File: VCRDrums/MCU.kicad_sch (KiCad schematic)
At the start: 45 parts, among them J901 SWD Header, SW901 RST, SW902 BOOT, U901 STM32F411RETx, Y901 16MHz, Y902 32.768kHZ

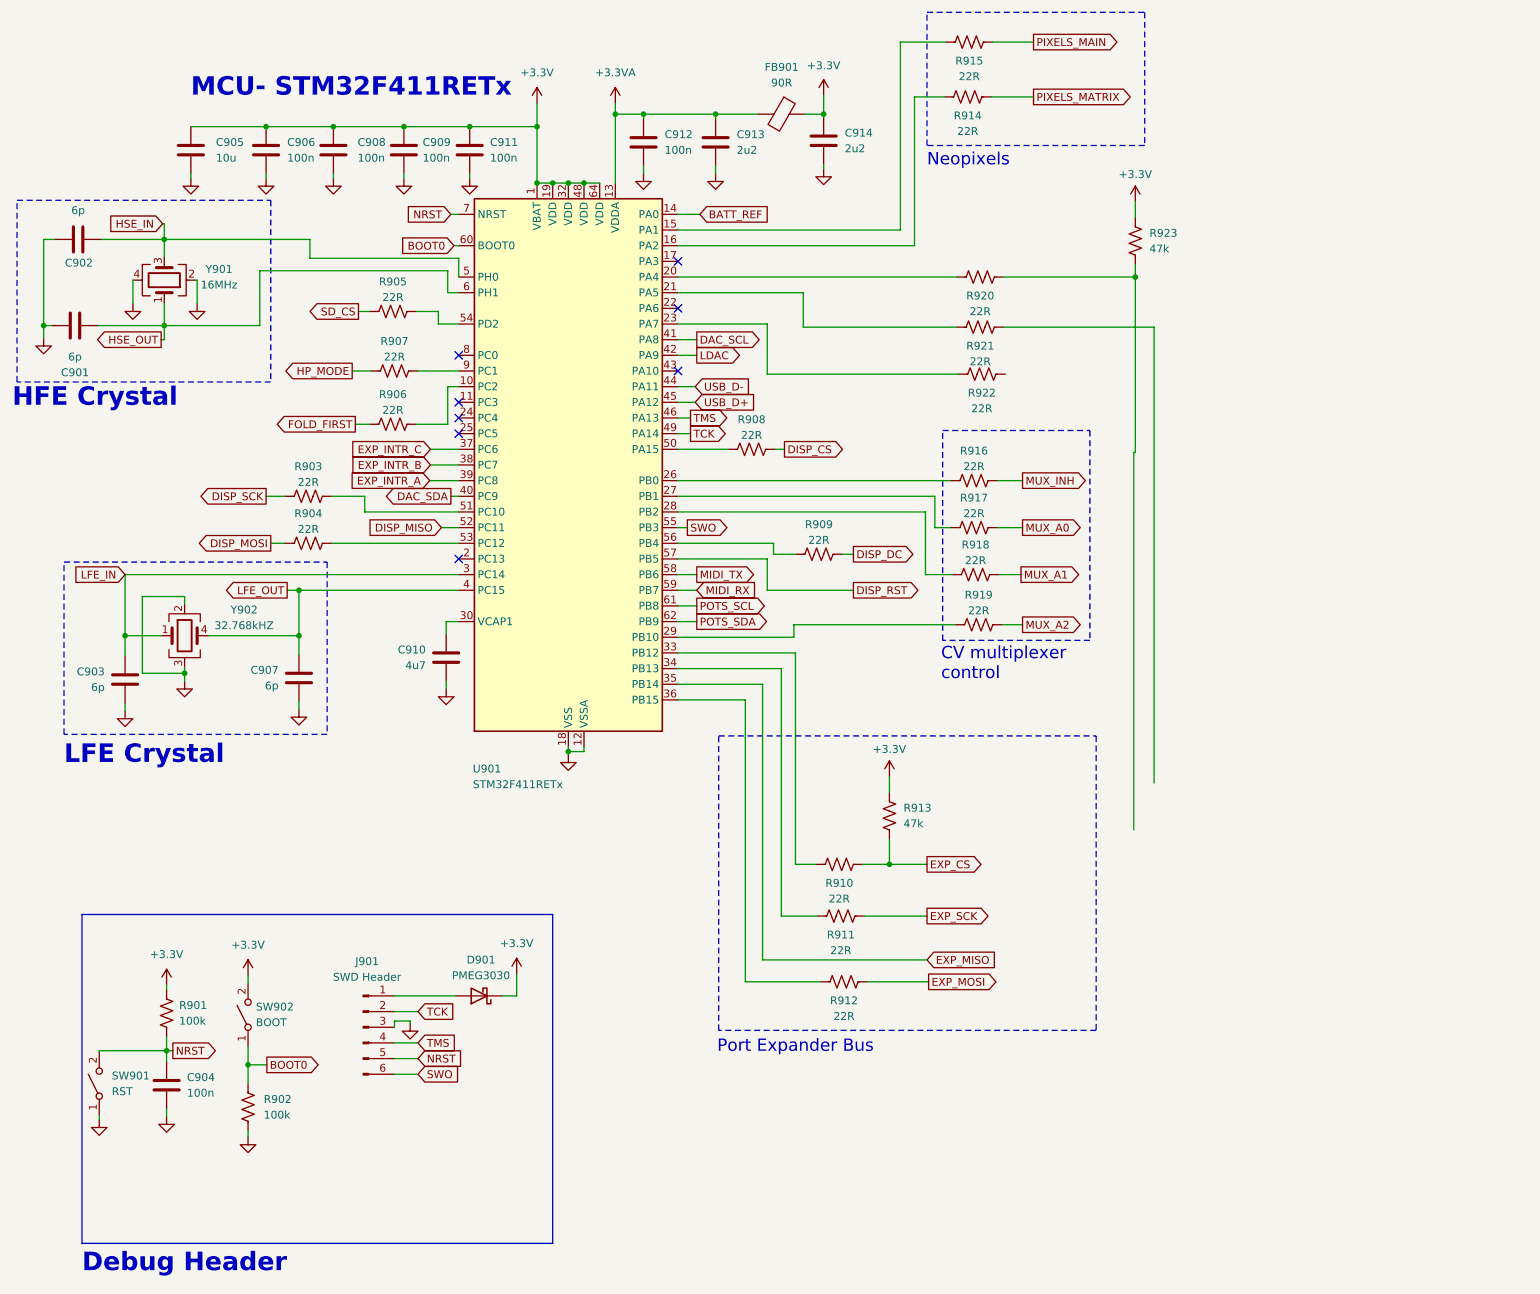
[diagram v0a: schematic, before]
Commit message: firmware boilerplate
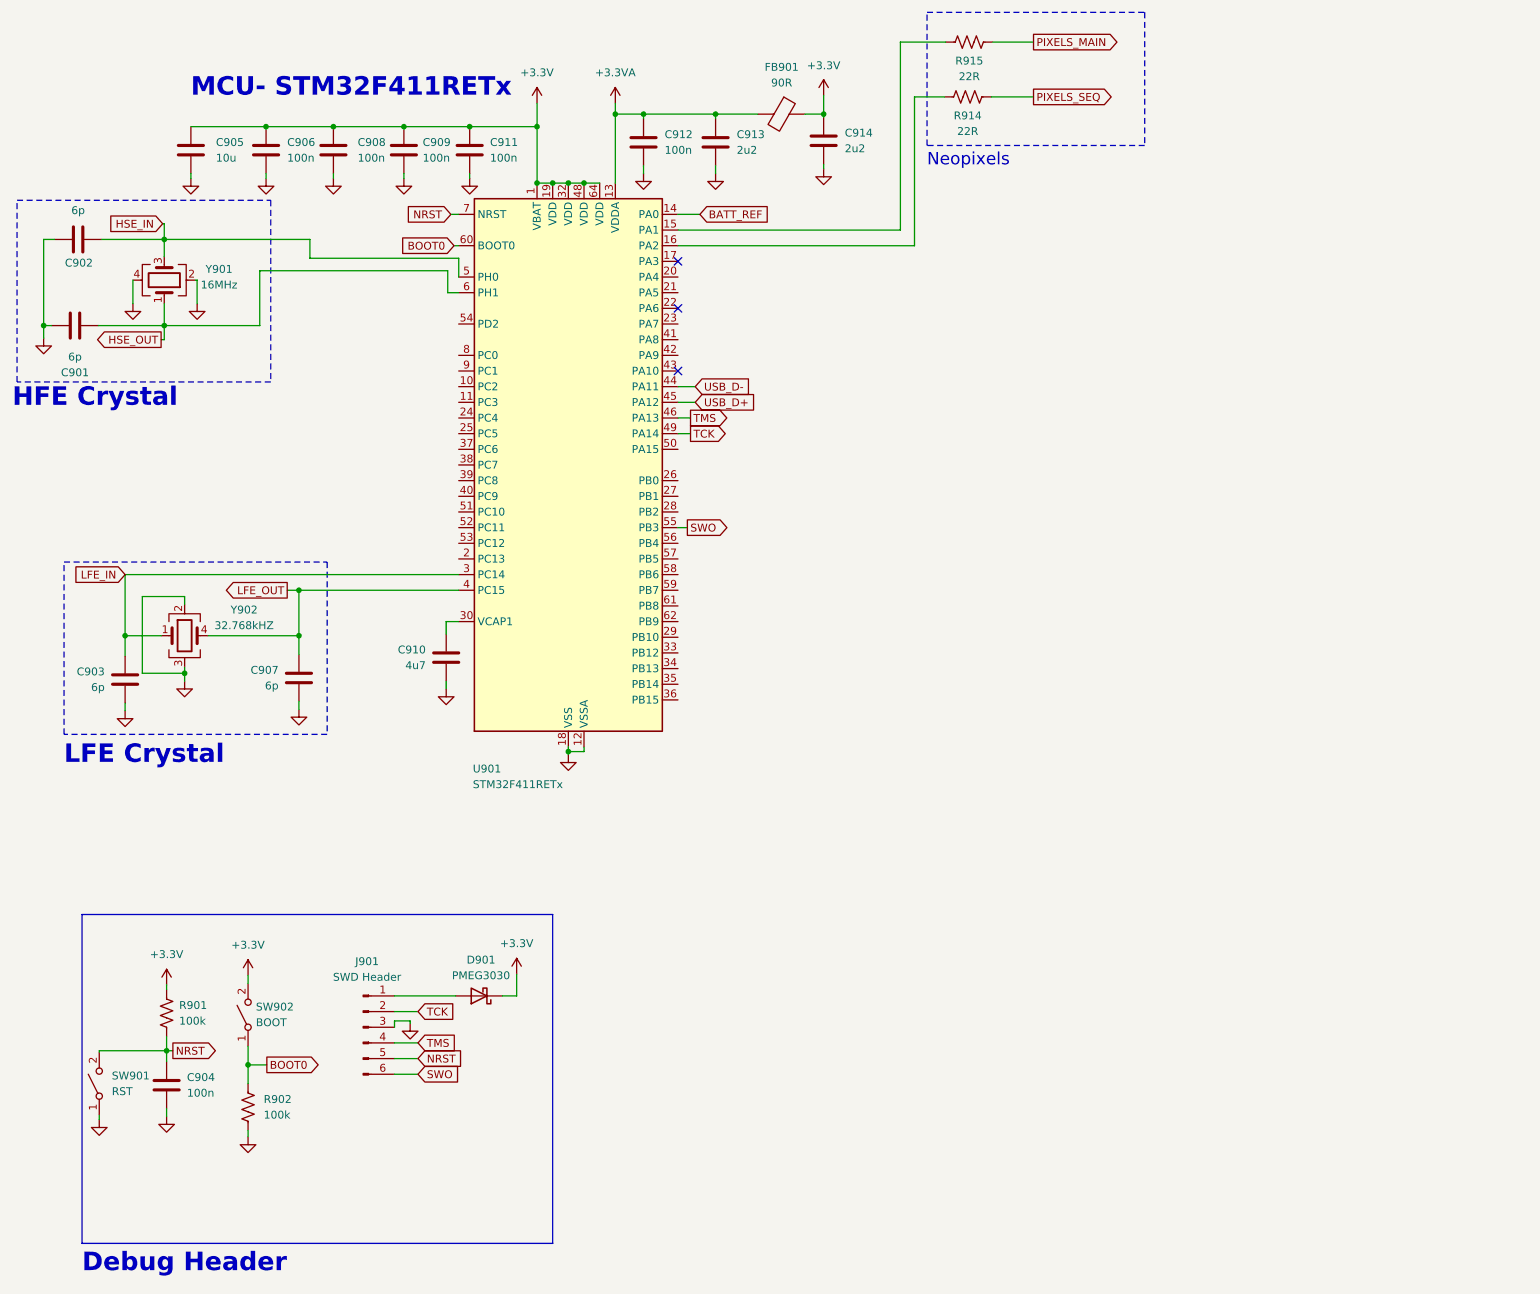
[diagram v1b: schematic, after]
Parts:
- removed R903, R904, R905, R906, R907, R908, R909, R910, R911, R912, R916, R917, R918, R919, R920, R921, R922: 22R, Resistor_SMD:R_0805_2012Metric, symbol Device:R_US
- removed R913, R923: 47k, Resistor_SMD:R_0805_2012Metric, symbol Device:R_US
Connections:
- net DAC_SCL: no longer names the net of U901.41 (PA8)
- net DAC_SDA: no longer names the net of U901.40 (PC9)
- net DISP_MISO: no longer names the net of U901.52 (PC11)
- net DISP_RST: no longer names the net of U901.57 (PB5)
- net EXP_INTR_A: no longer names the net of U901.39 (PC8)
- net EXP_INTR_B: no longer names the net of U901.38 (PC7)
- net EXP_INTR_C: no longer names the net of U901.37 (PC6)
- net EXP_MISO: no longer names the net of U901.35 (PB14)
- net LDAC: no longer names the net of U901.42 (PA9)
- net MIDI_RX: no longer names the net of U901.59 (PB7)
- net MIDI_TX: no longer names the net of U901.58 (PB6)
- net PIXELS_MATRIX renamed PIXELS_SEQ
- net POTS_SCL: no longer names the net of U901.61 (PB8)
- net POTS_SDA: no longer names the net of U901.62 (PB9)
- no-connect marks 8 -> 3
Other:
- note removed: "CV multiplexer control"
- note removed: "Port Expander Bus"

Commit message: compressor muxes and balanced out
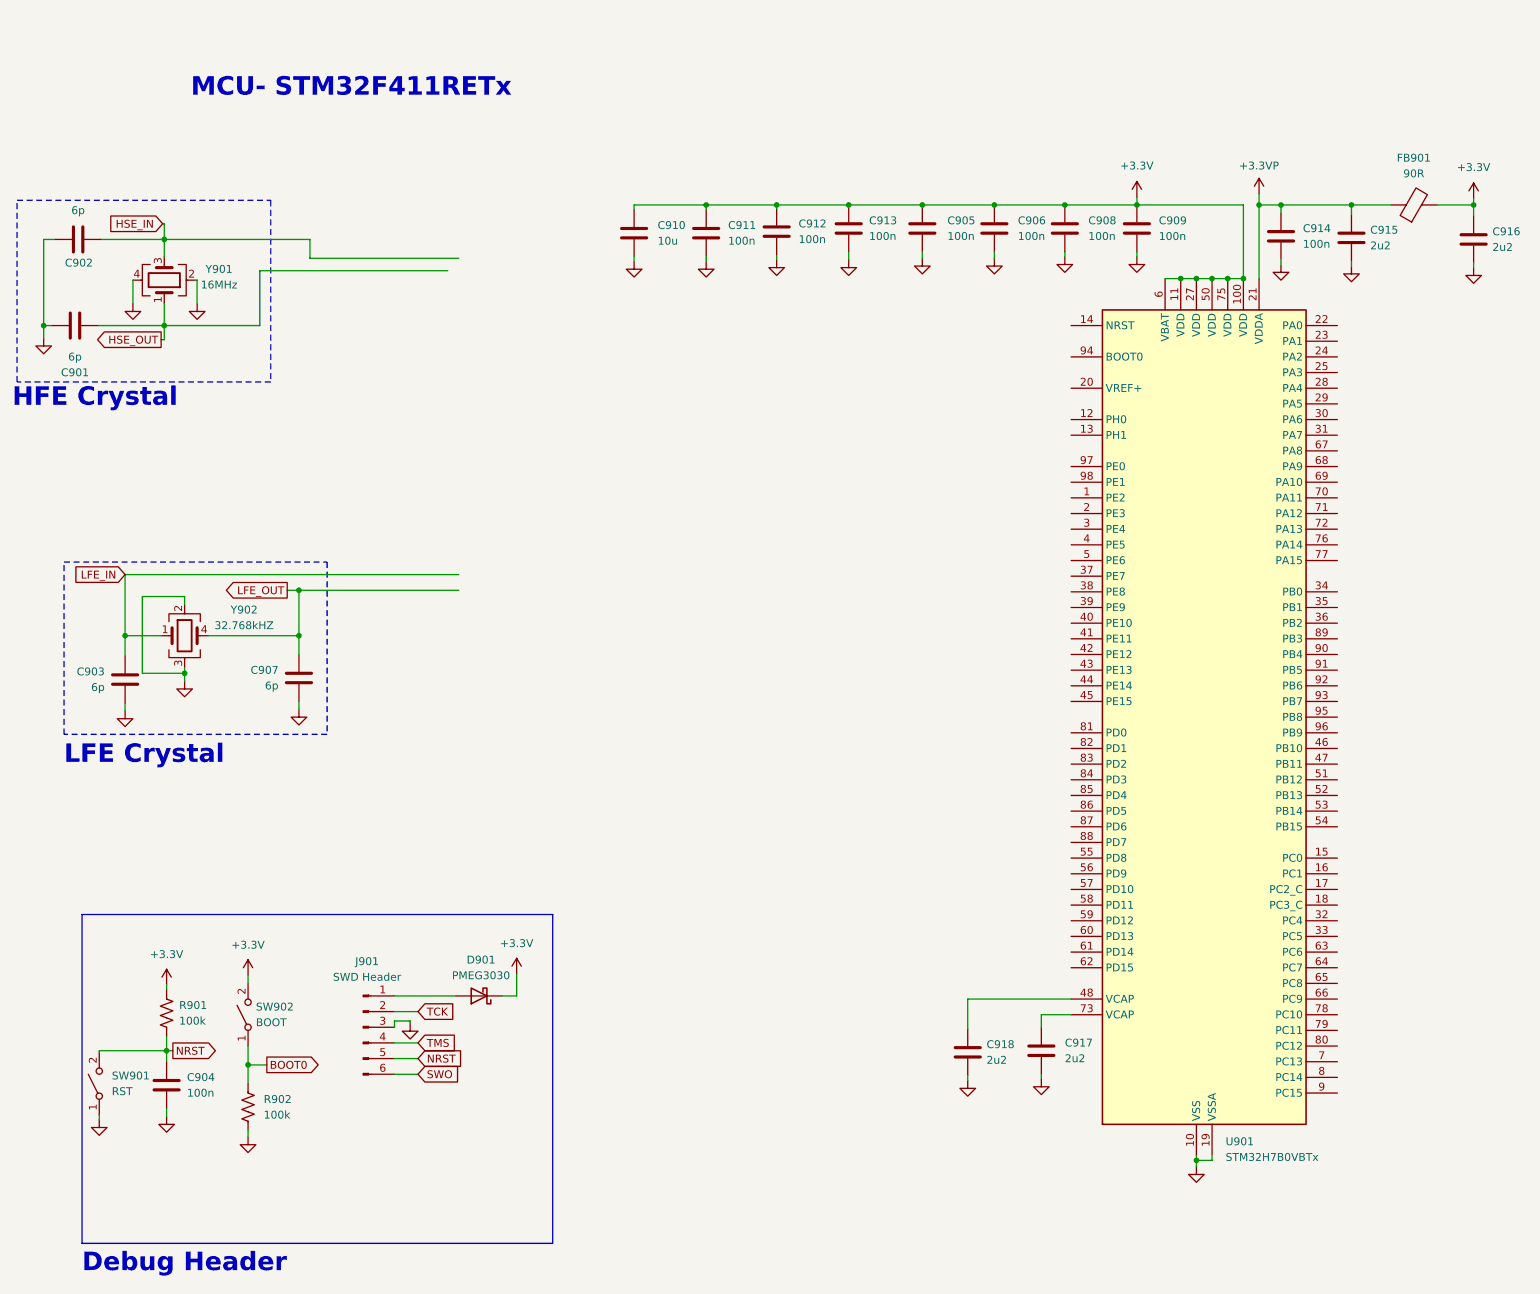
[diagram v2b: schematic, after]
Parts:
- removed R914, R915: 22R, Resistor_SMD:R_0805_2012Metric, symbol Device:R_US
- removed U901: STM32F411RETx, Package_QFP:LQFP-64_10x10mm_P0.5mm, symbol MCU_ST_STM32F4:STM32F411RETx
- added C915, C916, C917, C918: 2u2, symbol Device:C
- added U901: STM32H7B0VBTx, Package_QFP:LQFP-100_14x14mm_P0.5mm, symbol MCU_ST_STM32H7:STM32H7B0VBTx
- C905: value 10u -> 100n; footprint Capacitor_SMD:C_0805_2012Metric -> (none)
- C906, C908, C909, C911, C912: footprint Capacitor_SMD:C_0805_2012Metric -> (none)
- C910: value 4u7 -> 10u; footprint Capacitor_SMD:C_0805_2012Metric -> (none)
- C913, C914: value 2u2 -> 100n; footprint Capacitor_SMD:C_0805_2012Metric -> (none)
- FB901: footprint Inductor_SMD:L_0805_2012Metric -> (none)
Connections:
- net +3.3VA is gone; now on net +3.3V: C912.1, C913.1, FB901.2
- net +3.3V: now also C910.1, C916.1, U901.100 (VDD), U901.11 (VDD), U901.27 (VDD), U901.50 (VDD), U901.6 (VBAT), U901.75 (VDD); no longer C914.1, FB901.1
- net GND: now also C915.2, C916.2, C917.2, C918.2, U901.10 (VSS), U901.19 (VSSA), U901.26 (VSS), U901.49 (VSS), U901.74 (VSS), U901.99 (VSS)
- new net: C918.1, U901.48 (VCAP)
- new net: C917.1, U901.73 (VCAP)
- new net +3.3VP: C914.1, C915.1, FB901.1, U901.21 (VDDA)
- no-connect marks 3 -> 0
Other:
- note removed: "Neopixels"

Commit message: compressor schem and schematic
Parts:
- C905, C906, C908, C909, C910, C911, C912, C913, C914, C915, C916, C917, C918: footprint (none) -> Capacitor_SMD:C_0805_2012Metric
- FB901: footprint (none) -> Resistor_SMD:R_0805_2012Metric
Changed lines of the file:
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@@
 			)
 		)
-		(property "Footprint" ""
+		(property "Footprint" "Capacitor_SMD:C_0805_2012Metric"
 			(at 163.2712 55.118 0)
 			(effects
@@
 			)
 		)
-		(property "Footprint" ""
+		(property "Footprint" "Capacitor_SMD:C_0805_2012Metric"
 			(at 128.2192 55.88 0)
 			(effects
@@
 			)
 		)
-		(property "Footprint" ""
+		(property "Footprint" "Capacitor_SMD:C_0805_2012Metric"
 			(at 170.6372 188.722 0)
 			(effects
@@
 			)
 		)
-		(property "Footprint" ""
+		(property "Footprint" "Capacitor_SMD:C_0805_2012Metric"
 			(at 186.3852 55.118 0)
 			(effects
@@
 			)
 		)
-		(property "Footprint" ""
+		(property "Footprint" "Capacitor_SMD:C_0805_2012Metric"
 			(at 182.5752 188.468 0)
 			(effects
@@
 			)
 		)
-		(property "Footprint" ""
+		(property "Footprint" "Capacitor_SMD:C_0805_2012Metric"
 			(at 221.4372 56.388 0)
 			(effects
@@
 			)
 		)
-		(property "Footprint" ""
+		(property "Footprint" "Capacitor_SMD:C_0805_2012Metric"
 			(at 139.6492 55.626 0)
 			(effects
@@
 			)
 		)
-		(property "Footprint" ""
+		(property "Footprint" "Capacitor_SMD:C_0805_2012Metric"
 			(at 198.0692 55.118 0)
 			(effects
@@
 			)
 		)
-		(property "Footprint" ""
+		(property "Footprint" "Capacitor_SMD:C_0805_2012Metric"
 			(at 116.5352 55.88 0)
 			(effects
@@
 			)
 		)
-		(property "Footprint" ""
+		(property "Footprint" "Resistor_SMD:R_0805_2012Metric"
 			(at 242.062 49.276 90)
 			(effects
@@
 			)
 		)
-		(property "Footprint" ""
+		(property "Footprint" "Capacitor_SMD:C_0805_2012Metric"
 			(at 252.6792 56.896 0)
 			(effects
@@
 			)
 		)
-		(property "Footprint" ""
+		(property "Footprint" "Capacitor_SMD:C_0805_2012Metric"
 			(at 151.3332 55.118 0)
 			(effects
@@
 			)
 		)
-		(property "Footprint" ""
+		(property "Footprint" "Capacitor_SMD:C_0805_2012Metric"
 			(at 232.8672 56.642 0)
 			(effects
@@
 			)
 		)
-		(property "Footprint" ""
+		(property "Footprint" "Capacitor_SMD:C_0805_2012Metric"
 			(at 174.9552 55.118 0)
 			(effects
